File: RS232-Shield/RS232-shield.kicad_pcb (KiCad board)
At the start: 2 copper layers, 34.3 x 48.3 mm, 12 parts, among them J1 DB9_Female_MountingHoles, U1 WeMos_D1_mini, U2 MAX3232

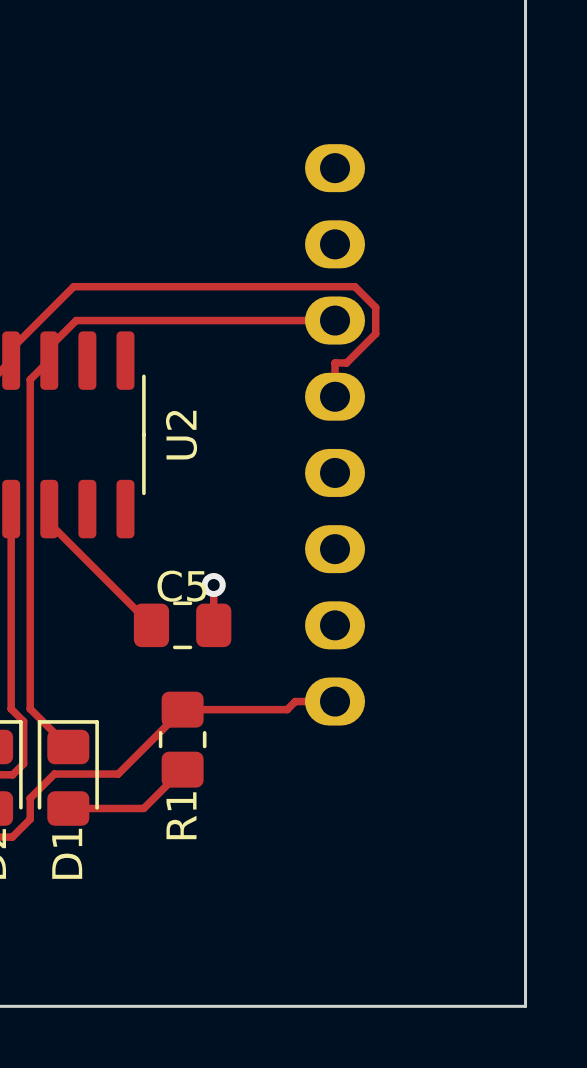
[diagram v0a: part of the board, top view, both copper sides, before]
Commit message: Add board name to silkscreen
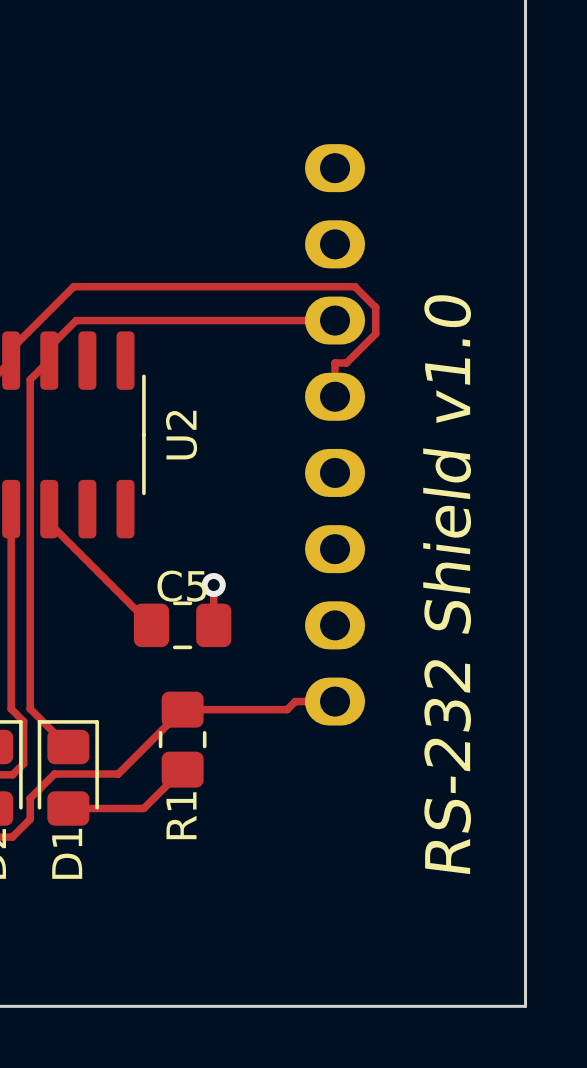
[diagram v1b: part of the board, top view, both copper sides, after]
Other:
- board text added: "RS-232 Shield v1.0"
